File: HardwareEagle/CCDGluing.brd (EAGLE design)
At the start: 160 x 100 mm, 8 parts, among them X1 BU-SMA-G

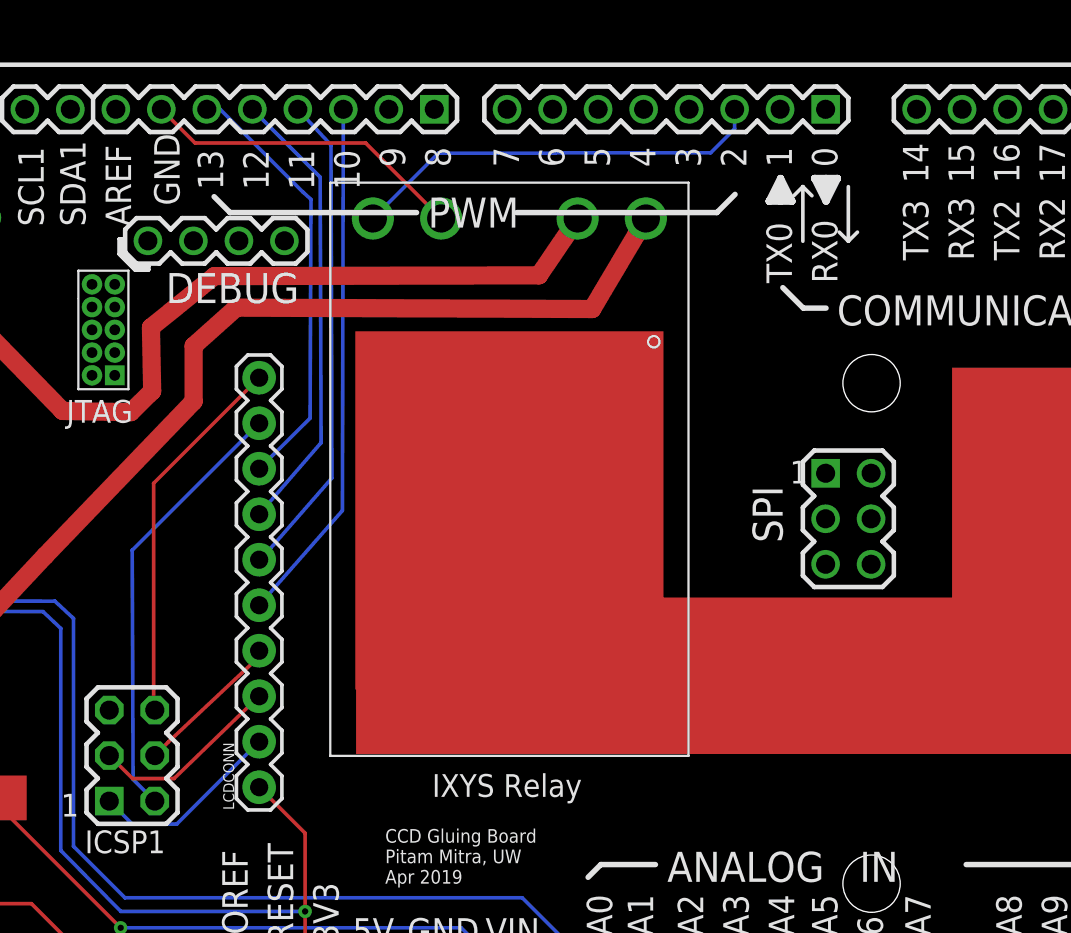
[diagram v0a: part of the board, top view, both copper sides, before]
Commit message: Fixed the design to use the correct SPI port on the due. Blame the documentation for being wrong.
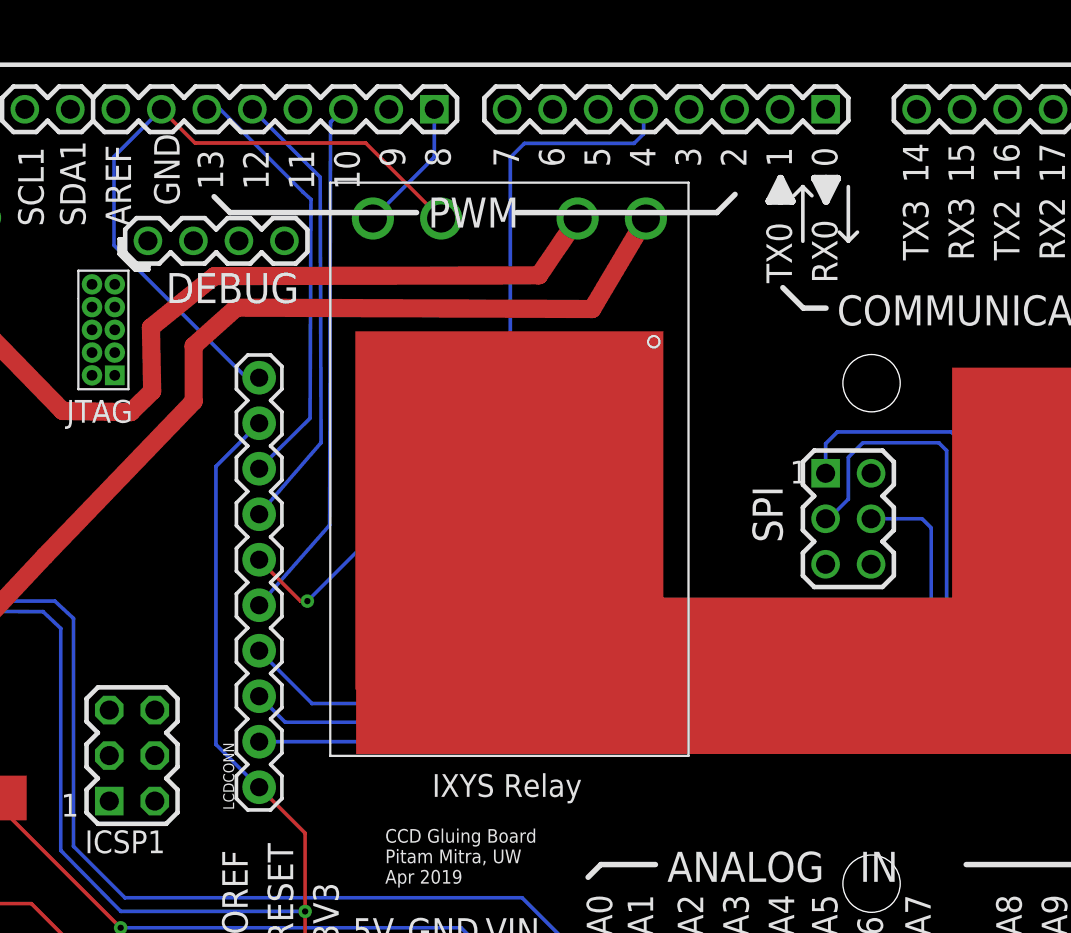
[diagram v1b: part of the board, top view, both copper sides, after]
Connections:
- removed net N$1: ARDUINO_DUE1.GND_ICSP1, LCDCONN.10
- removed net N$5: ARDUINO_DUE1.2, K1.4CTR+
- removed net N$6: ARDUINO_DUE1.GND_4, K1.3CTR-
- removed net VCC: ARDUINO_DUE1.5V_ICSP1, LCDCONN.9
- new net 4CTR+: ARDUINO_DUE1.8, K1.4CTR+
- new net GND: ARDUINO_DUE1.GND_4, K1.3CTR-, LCDCONN.10
- net 3.3V: now also LCDCONN.9
- net CLK: now also ARDUINO_DUE1.SPCK; no longer ARDUINO_DUE1.SCK2
- net CRD_CS: now also ARDUINO_DUE1.4; no longer ARDUINO_DUE1.11
- net CRD_MISO: now also ARDUINO_DUE1.MISO; no longer ARDUINO_DUE1.MISO2
- net MOSI: now also ARDUINO_DUE1.MOSI; no longer ARDUINO_DUE1.MOSI2
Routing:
- net CRD_MISO: track 10.8 -> 64.0 mm
- net CLK: track 10.8 -> 62.0 mm
- net MOSI: track 8.35 -> 50.1 mm
- net GND: track 0.00 -> 38.0 mm
- net VCC: track 24.5 -> 0.00 mm
- net N$5: track 23.4 -> 0.00 mm
- net 3.3V: track 63.6 -> 86.0 mm
- net N$1: track 21.0 -> 0.00 mm
- net N$6: track 18.1 -> 0.00 mm
- net CRD_CS: track 27.4 -> 42.5 mm, vias 0 -> 1
- net 4CTR+: track 0.00 -> 7.52 mm

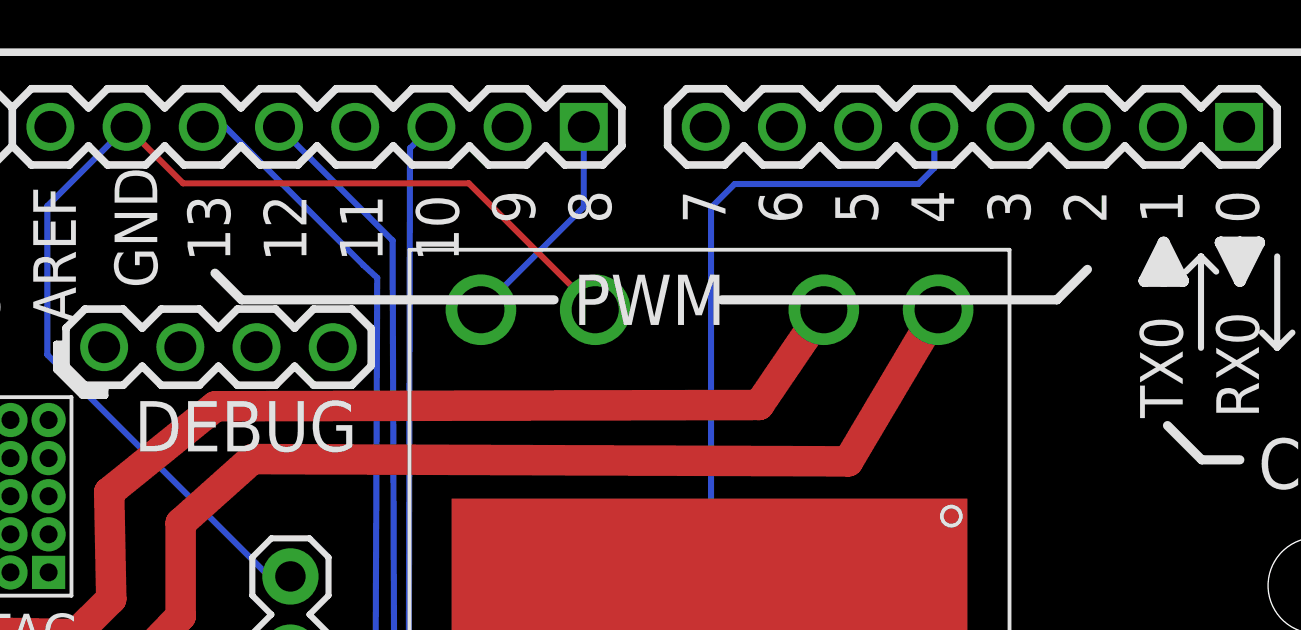
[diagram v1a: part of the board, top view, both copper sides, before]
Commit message: Added current limit resistor.
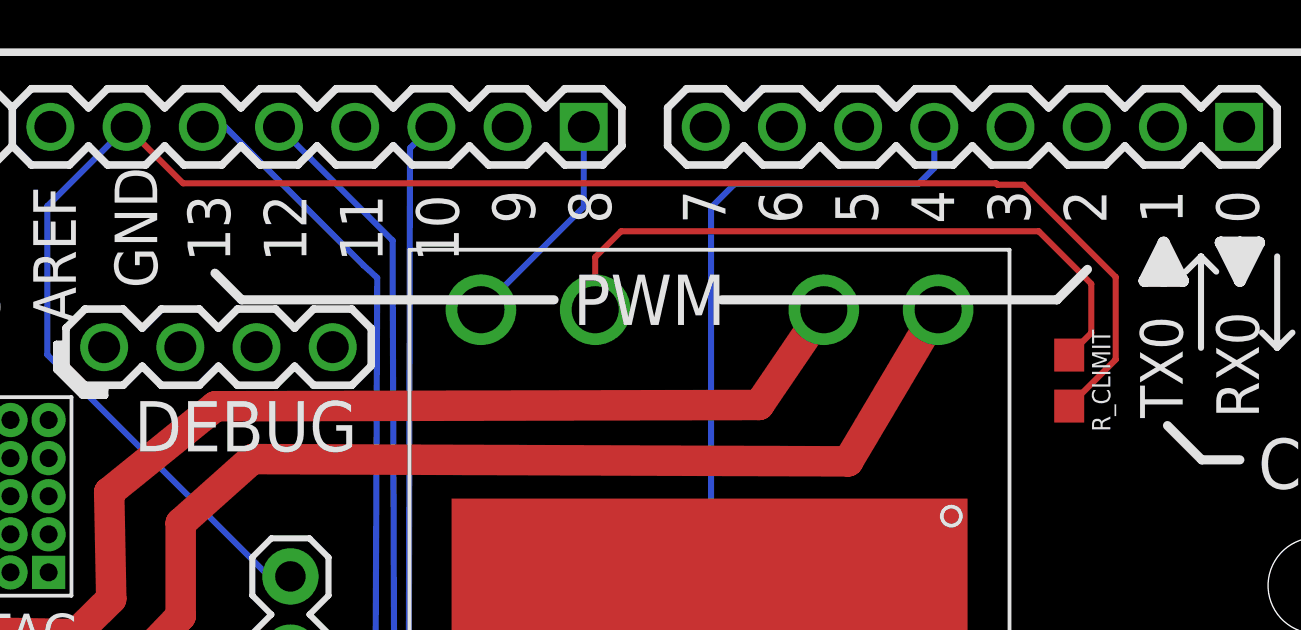
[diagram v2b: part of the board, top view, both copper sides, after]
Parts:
- added R_CLIMIT: 150, SparkFun-Resistors:0603
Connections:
- new net N$1: K1.3CTR-, R_CLIMIT.1
- net GND: now also R_CLIMIT.2; no longer K1.3CTR-
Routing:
- net N$1: track 0.00 -> 22.1 mm
- net GND: track 38.0 -> 59.8 mm
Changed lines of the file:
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@@
 <attribute name="VALUE" x="32.476159375" y="72.7546" size="1.6764" layer="27" font="vector" ratio="13" rot="SR270"/>
+</element>
+<element name="R_CLIMIT" library="SparkFun-Resistors" library_urn="urn:adsk.eagle:library:532" package="0603" package3d_urn="urn:adsk.eagle:package:39650/1" value="150" x="90.7288" y="64.9478" smashed="yes" rot="R270">
+<attribute name="NAME" x="91.4908" y="64.9478" size="0.6096" layer="25" font="vector" ratio="20" rot="R270" align="bottom-center"/>
+<attribute name="PROD_ID" value="RES-11028" x="90.7288" y="64.9478" size="1.778" layer="27" rot="R270" display="off"/>
+<attribute name="VALUE" x="89.9668" y="64.9478" size="0.6096" layer="27" font="vector" ratio="20" rot="R270" align="top-center"/>
 </element>
 </elements>
@@
 <signal name="GND">
 <contactref element="LCDCONN" pad="10"/>
-<contactref element="K1" pad="3CTR-"/>
 <contactref element="ARDUINO_DUE1" pad="GND_4"/>
-<wire x1="74.93" y1="67.31" x2="70.716" y2="71.524" width="0.2032" layer="1"/>
 <wire x1="61.191" y1="71.524" x2="59.309" y2="73.406" width="0.2032" layer="1"/>
-<wire x1="70.716" y1="71.524" x2="61.191" y2="71.524" width="0.2032" layer="1"/>
 <wire x1="59.309" y1="73.406" x2="56.6674" y2="70.7644" width="0.2032" layer="16"/>
 <wire x1="56.6674" y1="70.7644" x2="56.6674" y2="65.8114" width="0.2032" layer="16"/>
 <wire x1="56.6674" y1="65.8114" x2="64.0588" y2="58.42" width="0.2032" layer="16"/>
 <wire x1="64.0588" y1="58.42" x2="64.77" y2="58.42" width="0.2032" layer="16"/>
+<contactref element="R_CLIMIT" pad="2"/>
+<wire x1="61.191" y1="71.524" x2="88.2928" y2="71.524" width="0.2032" layer="1"/>
+<wire x1="88.2928" y1="71.524" x2="88.3412" y2="71.4756" width="0.2032" layer="1"/>
+<wire x1="88.3412" y1="71.4756" x2="89.2048" y2="71.4756" width="0.2032" layer="1"/>
+<wire x1="92.2782" y1="65.6472" x2="90.7288" y2="64.0978" width="0.2032" layer="1"/>
+<wire x1="89.2048" y1="71.4756" x2="92.2782" y2="68.4022" width="0.2032" layer="1"/>
+<wire x1="92.2782" y1="68.4022" x2="92.2782" y2="65.6472" width="0.2032" layer="1"/>
 </signal>
 <signal name="3.3V">
@@
 <wire x1="64.7446" y1="35.56" x2="64.77" y2="35.56" width="0.2032" layer="16"/>
 </signal>
+<signal name="N$1">
+<contactref element="K1" pad="3CTR-"/>
+<contactref element="R_CLIMIT" pad="1"/>
+<wire x1="74.93" y1="67.31" x2="74.93" y2="69.0626" width="0.2032" layer="1"/>
+<wire x1="74.93" y1="69.0626" x2="75.7936" y2="69.9262" width="0.2032" layer="1"/>
+<wire x1="75.7936" y1="69.9262" x2="89.7128" y2="69.9262" width="0.2032" layer="1"/>
+<wire x1="89.7128" y1="69.9262" x2="91.4654" y2="68.1736" width="0.2032" layer="1"/>
+<wire x1="91.4654" y1="68.1736" x2="91.4654" y2="66.5344" width="0.2032" layer="1"/>
+<wire x1="91.4654" y1="66.5344" x2="90.7288" y2="65.7978" width="0.2032" layer="1"/>
+</signal>
 </signals>
